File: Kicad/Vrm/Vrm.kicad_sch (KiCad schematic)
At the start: 7 parts, among them J1 Screw_Terminal_01x04, J2 Screw_Terminal_01x04, J3 Screw_Terminal_01x02, Q1 ZVN4106F

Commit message: Updated Schematic
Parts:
- removed J1, J2: Screw_Terminal_01x04, symbol Connector:Screw_Terminal_01x04
- removed Q1: ZVN4106F, Package_TO_SOT_SMD:SOT-23, symbol Transistor_FET:ZVN4106F
- added C1, C4, C5: 100nF, symbol Device:C
- added C2, C?: 1uF, symbol Device:C
- added C3, C?: 10nF, symbol Device:C
- added C6: 4.7uF, symbol Device:C
- added J2: Screw_Terminal_01x02, symbol Connector:Screw_Terminal_01x02
- added J4: AVR-JTAG-10, symbol Connector:AVR-JTAG-10
- added Q1: 2N3704, Package_TO_SOT_THT:TO-92_Inline, symbol Transistor_BJT:2N3904
- added R2: 47k, symbol Device:R
- added SW1: Switch, symbol Switch:SW_Push
- R1: value 150 -> 1k
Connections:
- net GND: now also U?.31 (VSS), U?.47 (VSS), U?.63 (VSS), C1.2, C2.2, C3.2, C4.2, C5.2, C6.2, C?.2, C?.2, J4.3 (GND), J4.5 (GND), J4.9 (GND), Q1.1 (E), SW1.2
- net VDD: now also U?.1 (VBAT), U?.32 (VDD), U?.64 (VDD), C4.1, C5.1, C6.1, J4.1 (VDD)
- net Buzzer Module: now reaches U?.41 (PA8)
- net Buzzer Module: now also R2.2
- net at BZ.2 (+), R1.2: now also Q1.3 (C)
- net VDDA: now reaches U?.13 (VDDA)
- net VDDA: now also C2.1, C3.1, C?.1, C?.1
- net at U?.16 (PA2): now also J2.1 (__Servo_TX)
- net at U?.17 (PA3): now also J2.2 (__Servo_RX)
- net SWDIO: now reaches U?.46 (PA13)
- net SWDIO: now also J4.2 (SWDIO), J4.4 (SWCLK)
- net SWCLK: now reaches U?.49 (PA14)
- net NRST: now reaches U?.7 (NRST)
- net NRST: now also C1.1, J4.10 (NRST), SW1.1

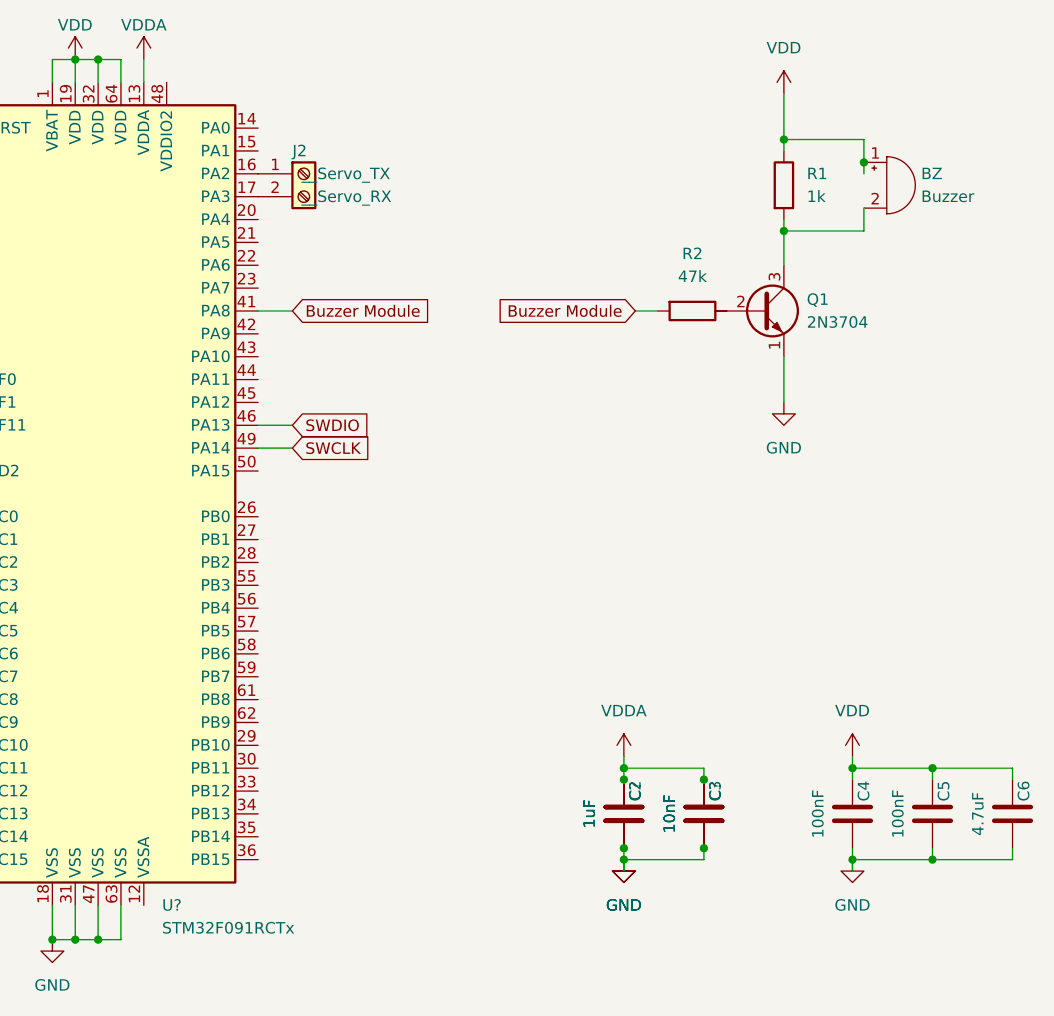
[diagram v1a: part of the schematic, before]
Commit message: Making Joe's PCB updates
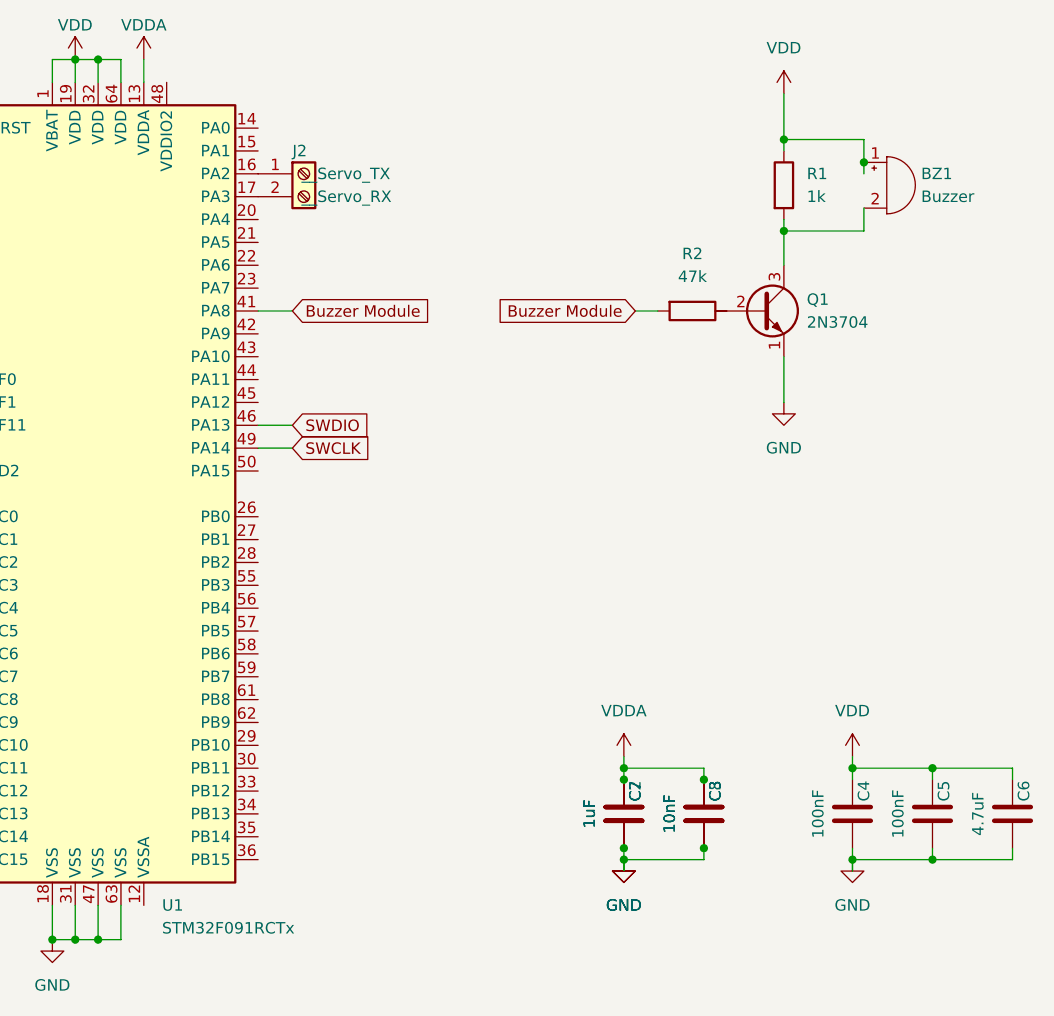
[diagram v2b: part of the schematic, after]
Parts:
- gave numbers to parts that had none: 3
- renumbered BZ to BZ1
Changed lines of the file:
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@@
   (symbol (lib_id "power:GND") (at 198.12 124.46 0) (unit 1)
     (in_bom yes) (on_board yes) (fields_autoplaced)
-    (property "Reference" "#PWR?" (id 0) (at 198.12 130.81 0)
+    (property "Reference" "#PWR0102" (id 0) (at 198.12 130.81 0)
       (effects (font (size 1.27 1.27)) hide)
     )
@@
   (symbol (lib_id "power:VDDA") (at 198.12 113.03 0) (unit 1)
     (in_bom yes) (on_board yes) (fields_autoplaced)
-    (property "Reference" "#PWR?" (id 0) (at 198.12 116.84 0)
+    (property "Reference" "#PWR0103" (id 0) (at 198.12 116.84 0)
       (effects (font (size 1.27 1.27)) hide)
     )
@@
   (symbol (lib_id "power:VDD") (at 137.16 35.56 0) (unit 1)
     (in_bom yes) (on_board yes)
-    (property "Reference" "#PWR?" (id 0) (at 137.16 39.37 0)
+    (property "Reference" "#PWR0111" (id 0) (at 137.16 39.37 0)
       (effects (font (size 1.27 1.27)) hide)
     )
@@
   (symbol (lib_id "power:GND") (at 67.31 58.42 90) (unit 1)
     (in_bom yes) (on_board yes) (fields_autoplaced)
-    (property "Reference" "#PWR?" (id 0) (at 73.66 58.42 0)
+    (property "Reference" "#PWR0110" (id 0) (at 73.66 58.42 0)
       (effects (font (size 1.27 1.27)) hide)
     )
@@
   (symbol (lib_id "Device:C") (at 198.12 119.38 0) (unit 1)
     (in_bom yes) (on_board yes)
-    (property "Reference" "C?" (id 0) (at 199.39 116.84 90))
+    (property "Reference" "C7" (id 0) (at 199.39 116.84 90))
     (property "Value" "1uF" (id 1) (at 194.31 119.38 90))
     (property "Footprint" "" (id 2) (at 199.0852 123.19 0)
@@
   (symbol (lib_id "MCU_ST_STM32F0:STM32F091RCTx") (at 142.24 83.82 0) (unit 1)
     (in_bom yes) (on_board yes) (fields_autoplaced)
-    (property "Reference" "U?" (id 0) (at 146.7994 129.54 0)
+    (property "Reference" "U1" (id 0) (at 146.7994 129.54 0)
       (effects (font (size 1.27 1.27)) (justify left))
     )
@@
   (symbol (lib_id "power:GND") (at 41.91 54.61 270) (mirror x) (unit 1)
     (in_bom yes) (on_board yes) (fields_autoplaced)
-    (property "Reference" "#PWR?" (id 0) (at 35.56 54.61 0)
+    (property "Reference" "#PWR0108" (id 0) (at 35.56 54.61 0)
       (effects (font (size 1.27 1.27)) hide)
     )
@@
   (symbol (lib_id "power:GND") (at 215.9 73.66 0) (unit 1)
     (in_bom yes) (on_board yes) (fields_autoplaced)
-    (property "Reference" "#PWR?" (id 0) (at 215.9 80.01 0)
+    (property "Reference" "#PWR0114" (id 0) (at 215.9 80.01 0)
       (effects (font (size 1.27 1.27)) hide)
     )
@@
   (symbol (lib_id "power:GND") (at 134.62 133.35 0) (unit 1)
     (in_bom yes) (on_board yes) (fields_autoplaced)
-    (property "Reference" "#PWR?" (id 0) (at 134.62 139.7 0)
+    (property "Reference" "#PWR0101" (id 0) (at 134.62 139.7 0)
       (effects (font (size 1.27 1.27)) hide)
     )
@@
   (symbol (lib_id "Device:C") (at 207.01 119.38 0) (unit 1)
     (in_bom yes) (on_board yes)
-    (property "Reference" "C?" (id 0) (at 208.28 116.84 90))
+    (property "Reference" "C8" (id 0) (at 208.28 116.84 90))
     (property "Value" "10nF" (id 1) (at 203.2 119.38 90))
     (property "Footprint" "" (id 2) (at 207.9752 123.19 0)
@@
   (symbol (lib_id "Device:Buzzer") (at 227.33 49.53 0) (unit 1)
     (in_bom yes) (on_board yes) (fields_autoplaced)
-    (property "Reference" "BZ" (id 0) (at 231.14 48.2599 0)
+    (property "Reference" "BZ1" (id 0) (at 231.14 48.2599 0)
       (effects (font (size 1.27 1.27)) (justify left))
     )
@@
   (symbol (lib_id "power:GND") (at 223.52 124.46 0) (unit 1)
     (in_bom yes) (on_board yes) (fields_autoplaced)
-    (property "Reference" "#PWR?" (id 0) (at 223.52 130.81 0)
+    (property "Reference" "#PWR0105" (id 0) (at 223.52 130.81 0)
       (effects (font (size 1.27 1.27)) hide)
     )
@@
   (symbol (lib_id "power:GND") (at 41.91 62.23 270) (mirror x) (unit 1)
     (in_bom yes) (on_board yes) (fields_autoplaced)
-    (property "Reference" "#PWR?" (id 0) (at 35.56 62.23 0)
+    (property "Reference" "#PWR0109" (id 0) (at 35.56 62.23 0)
       (effects (font (size 1.27 1.27)) hide)
     )
@@
   (symbol (lib_id "power:VDD") (at 215.9 39.37 0) (unit 1)
     (in_bom yes) (on_board yes) (fields_autoplaced)
-    (property "Reference" "#PWR?" (id 0) (at 215.9 43.18 0)
+    (property "Reference" "#PWR0113" (id 0) (at 215.9 43.18 0)
       (effects (font (size 1.27 1.27)) hide)
     )
@@
   (symbol (lib_id "power:GND") (at 86.36 82.55 0) (unit 1)
     (in_bom yes) (on_board yes) (fields_autoplaced)
-    (property "Reference" "#PWR?" (id 0) (at 86.36 88.9 0)
+    (property "Reference" "#PWR0107" (id 0) (at 86.36 88.9 0)
       (effects (font (size 1.27 1.27)) hide)
     )
@@
   (symbol (lib_id "power:GND") (at 198.12 124.46 0) (unit 1)
     (in_bom yes) (on_board yes) (fields_autoplaced)
-    (property "Reference" "#PWR?" (id 0) (at 198.12 130.81 0)
+    (property "Reference" "#PWR0104" (id 0) (at 198.12 130.81 0)
       (effects (font (size 1.27 1.27)) hide)
     )
@@
   (symbol (lib_id "power:VDD") (at 223.52 113.03 0) (unit 1)
     (in_bom yes) (on_board yes) (fields_autoplaced)
-    (property "Reference" "#PWR?" (id 0) (at 223.52 116.84 0)
+    (property "Reference" "#PWR0106" (id 0) (at 223.52 116.84 0)
       (effects (font (size 1.27 1.27)) hide)
     )
@@
   (symbol (lib_id "power:VDDA") (at 144.78 35.56 0) (unit 1)
     (in_bom yes) (on_board yes)
-    (property "Reference" "#PWR?" (id 0) (at 144.78 39.37 0)
+    (property "Reference" "#PWR0112" (id 0) (at 144.78 39.37 0)
       (effects (font (size 1.27 1.27)) hide)
     )
@@
   )
   (symbol_instances
+    (path "/5a1b213f-ef4e-4c44-bddb-806a07c27539"
+      (reference "#PWR0101") (unit 1) (value "GND") (footprint "")
+    )
     (path "/0d1fb268-0a24-4109-9c0e-09ad7b0de79a"
-      (reference "#PWR?") (unit 1) (value "GND") (footprint "")
+      (reference "#PWR0102") (unit 1) (value "GND") (footprint "")
     )
     (path "/314b93e4-6442-4273-806e-c2df96496ffd"
-      (reference "#PWR?") (unit 1) (value "VDDA") (footprint "")
+      (reference "#PWR0103") (unit 1) (value "VDDA") (footprint "")
+    )
+    (path "/d691fcd9-40f2-4bb5-82d3-025fd06cf914"
+      (reference "#PWR0104") (unit 1) (value "GND") (footprint "")
+    )
+    (path "/a4d4b8de-1c3b-4e08-a3a2-f514565c2bcf"
+      (reference "#PWR0105") (unit 1) (value "GND") (footprint "")
+    )
+    (path "/dc7ecea4-3726-403b-a7d2-ab0000ae2fc4"
+      (reference "#PWR0106") (unit 1) (value "VDD") (footprint "")
+    )
+    (path "/cee6d1ba-f71e-4e02-9cef-7a2783bb38f5"
+      (reference "#PWR0107") (unit 1) (value "GND") (footprint "")
+    )
+    (path "/4cf535d6-696b-4bd1-a7e2-126330c05267"
+      (reference "#PWR0108") (unit 1) (value "GND") (footprint "")
+    )
+    (path "/af222ff1-0979-4243-b425-e99dbe71a034"
+      (reference "#PWR0109") (unit 1) (value "GND") (footprint "")
+    )
+    (path "/3887017f-0bb1-4d6f-aee8-bc17d81061d4"
+      (reference "#PWR0110") (unit 1) (value "GND") (footprint "")
     )
     (path "/344ade11-ae7e-4a28-83ea-d4df5fb52a76"
-      (reference "#PWR?") (unit 1) (value "VDD") (footprint "")
-    )
-    (path "/3887017f-0bb1-4d6f-aee8-bc17d81061d4"
-      (reference "#PWR?") (unit 1) (value "GND") (footprint "")
-    )
-    (path "/4cf535d6-696b-4bd1-a7e2-126330c05267"
-      (reference "#PWR?") (unit 1) (value "GND") (footprint "")
+      (reference "#PWR0111") (unit 1) (value "VDD") (footprint "")
+    )
+    (path "/e89bdbcb-3e14-443b-9be0-a0fcfc6a9fcc"
+      (reference "#PWR0112") (unit 1) (value "VDDA") (footprint "")
+    )
+    (path "/c0717718-44d8-4988-bec8-faeaafa8e45a"
+      (reference "#PWR0113") (unit 1) (value "VDD") (footprint "")
     )
     (path "/4fc9de57-db53-4765-a283-4ab5d54b31ca"
-      (reference "#PWR?") (unit 1) (value "GND") (footprint "")
-    )
-    (path "/5a1b213f-ef4e-4c44-bddb-806a07c27539"
-      (reference "#PWR?") (unit 1) (value "GND") (footprint "")
-    )
-    (path "/a4d4b8de-1c3b-4e08-a3a2-f514565c2bcf"
-      (reference "#PWR?") (unit 1) (value "GND") (footprint "")
-    )
-    (path "/af222ff1-0979-4243-b425-e99dbe71a034"
-      (reference "#PWR?") (unit 1) (value "GND") (footprint "")
-    )
-    (path "/c0717718-44d8-4988-bec8-faeaafa8e45a"
-      (reference "#PWR?") (unit 1) (value "VDD") (footprint "")
-    )
-    (path "/cee6d1ba-f71e-4e02-9cef-7a2783bb38f5"
-      (reference "#PWR?") (unit 1) (value "GND") (footprint "")
-    )
-    (path "/d691fcd9-40f2-4bb5-82d3-025fd06cf914"
-      (reference "#PWR?") (unit 1) (value "GND") (footprint "")
-    )
-    (path "/dc7ecea4-3726-403b-a7d2-ab0000ae2fc4"
-      (reference "#PWR?") (unit 1) (value "VDD") (footprint "")
-    )
-    (path "/e89bdbcb-3e14-443b-9be0-a0fcfc6a9fcc"
-      (reference "#PWR?") (unit 1) (value "VDDA") (footprint "")
+      (reference "#PWR0114") (unit 1) (value "GND") (footprint "")
     )
     (path "/831f34f7-bb54-4f24-afae-cc9c189e51b1"
-      (reference "BZ") (unit 1) (value "Buzzer") (footprint "")
+      (reference "BZ1") (unit 1) (value "Buzzer") (footprint "")
     )
     (path "/0a71a939-e8b9-4da2-9f24-7433acb72f68"
@@
     )
     (path "/3979318f-652f-4f7d-8b2c-ea857095cdaf"
-      (reference "C?") (unit 1) (value "1uF") (footprint "")
+      (reference "C7") (unit 1) (value "1uF") (footprint "")
     )
     (path "/69c02132-dc91-44dd-9cbc-9915f6e41fc2"
-      (reference "C?") (unit 1) (value "10nF") (footprint "")
+      (reference "C8") (unit 1) (value "10nF") (footprint "")
     )
     (path "/bd6963f7-b6cc-46fc-82ce-120a458b4655"
@@
     )
     (path "/464ec877-0d2b-4741-aae7-258d04e12cd6"
-      (reference "U?") (unit 1) (value "STM32F091RCTx") (footprint "Package_QFP:LQFP-64_10x10mm_P0.5mm")
-    )
-  )
+      (reference "U1") (unit 1) (value "STM32F091RCTx") (footprint "Package_QFP:LQFP-64_10x10mm_P0.5mm")
+    )
+  )

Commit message: Updated schematic
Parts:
- removed BZ1: Buzzer, symbol Device:Buzzer
- removed J2, J3: Screw_Terminal_01x02, symbol Connector:Screw_Terminal_01x02
- removed J4: AVR-JTAG-10, symbol Connector:AVR-JTAG-10
- removed Q1: 2N3704, Package_TO_SOT_THT:TO-92_Inline, symbol Transistor_BJT:2N3904
- added BZ1: PS1240P02BT, digikey-footprints:Piezo_Transducer_THT_PS1240P02BT, symbol dk_Alarms-Buzzers-and-Sirens:PS1240P02BT
- added C9: 100nF, symbol Device:C
- added C?: 1uF, symbol Device:C
- added C?: 2.2uF, symbol Device:C
- added C?: 10nF, symbol Device:C
- added J1: Screw_Terminal_01x05, symbol Connector:Screw_Terminal_01x05
- added J2: AVR-JTAG-10, symbol Connector:AVR-JTAG-10
- added J3: Screw_Terminal_01x03, symbol Connector:Screw_Terminal_01x03
- added J4: Screw_Terminal_01x04, symbol Connector:Screw_Terminal_01x04
- added L1, L2: 100uH, symbol pspice:INDUCTOR
- added Q1: FMMT458TA - SOT23, digikey-footprints:SOT-23-3, symbol dk_Transistors-Bipolar-BJT-Single:FMMT458TA
- added R3: 1k, symbol Device:R
- added R4: 47k, symbol Device:R
- added U? (x2): LTC3638, Package_SO:Linear_MSOP-12-16-1EP_3x4mm_P0.5mm, symbol Regulator_Switching:LTC3638
- C1: value 100nF -> 10uF
- C2: value 1uF -> 10uF
- C3: value 10nF -> 1uF
- C4: value 100nF -> 10nF
- C6: value 4.7uF -> 100nF
- C7: value 1uF -> 4.7uF
- C8: value 10nF -> 2.2uF
- R1: value 1k -> 10k
- R2: value 47k -> 10k
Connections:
- net Buzzer Module: now also R4.2; no longer R2.2
- net GND: now also R1.1, U1.12 (VSSA), C9.2, C?.2, C?.2, C?.2, J2.3 (GND), J2.5 (GND), J2.9 (GND), J3.3 (Pin_3), J4.1 (Pin_1), Q1.2 (E)
- net NRST: now also R2.2, C9.1, J2.10 (NRST); no longer C1.1
- net SWDIO: now also J2.2 (SWDIO), J2.4 (SWCLK)
- net VDD: now also C7.1; no longer C4.1, R1.1, U1.1 (VBAT), U1.19 (VDD), U1.32 (VDD), U1.64 (VDD)
- net VDDA: now also C4.1, C?.1, C?.1; no longer C2.1, C7.1, C8.1, U1.13 (VDDA)
- net at U1.51 (PC10): now also J4.4 (Pin_4)
- net at U1.52 (PC11): now also J4.3 (Pin_3)
- net at U1.16 (PA2): now also J3.1 (Pin_1)
- net at U1.17 (PA3): now also J3.2 (Pin_2)
- net GPIO1: now reaches U1.23 (PA7)
- net GPIO1: now also J1.1 (Pin_1)
- net GPIO2: now reaches U1.24 (PC4)
- net GPIO2: now also J1.2 (Pin_2)
- net GPIO3: now reaches U1.25 (PC5)
- net GPIO3: now also J1.3 (Pin_3)
- net GPIO4: now reaches U1.26 (PB0)
- net GPIO4: now also J1.4 (Pin_4)
- net GPIO5: now reaches U1.27 (PB1)
- net GPIO5: now also J1.5 (Pin_5)
- net 3.3V: now reaches U1.48 (VDDIO2)
- net 3.3V: now also C1.1, R2.1, U1.1 (VBAT), U1.13 (VDDA), U1.19 (VDD), U1.32 (VDD), U1.64 (VDD), J2.1 (VDD), L2.2, U?.1 (SW)
- net at U1.60 (PF11): now also R1.2
- new net: L1.1, U?.6 (VOUT)
- new net: BZ1.2, Q1.3 (C), R3.2
- new net: Q1.1 (B), R4.1
- new net: L2.1, U?.6 (VOUT)
- new net +5V: C8.1, U?.2 (VIN), U?.5 (RUN)
- new net +7.5V: C?.1, U?.2 (VIN), U?.5 (RUN)
- new net 5V: BZ1.1, C2.1, L1.2, R3.1, U?.1 (SW)
